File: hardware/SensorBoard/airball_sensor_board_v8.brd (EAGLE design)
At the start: 88.9 x 38.1 mm, 61 parts, among them IC1 CP2102, J2 USB Female Type C Connector, T1 BC846, T2 BC846, U1 BQ24075, U2 BQ27441-G1, U3 BMP388, U4 ESP-WROOM-32, U7 SP0503BAHT

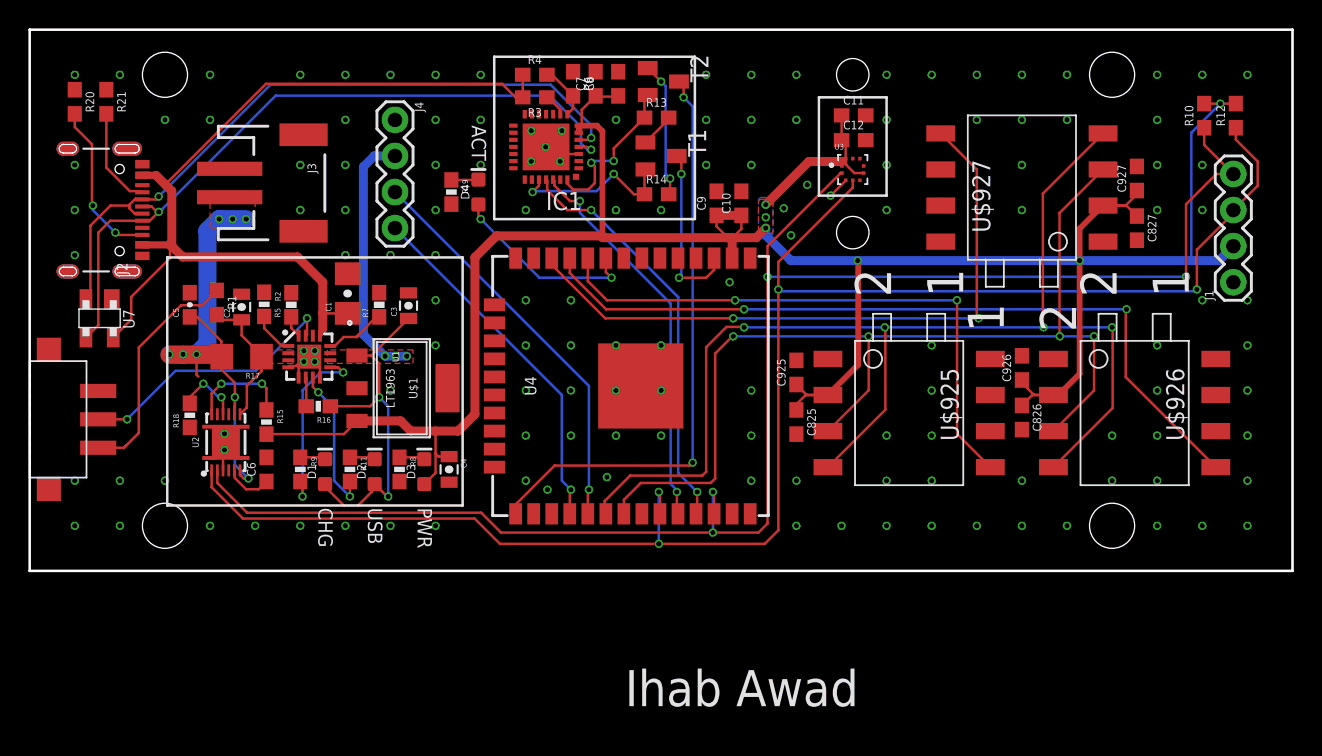
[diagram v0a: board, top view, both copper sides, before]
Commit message: Next rev of sensor board v8
Moved pressure sensors to more accessible location; added a pullup and
capacitor for one of the ESP32 pins for USB access; changed pressure
sensor to the newer BMP390; changed pressure sensor pads to support
either SMD or thru-hole variants; cleaned up the locations of the
barometer and its mounting holes.
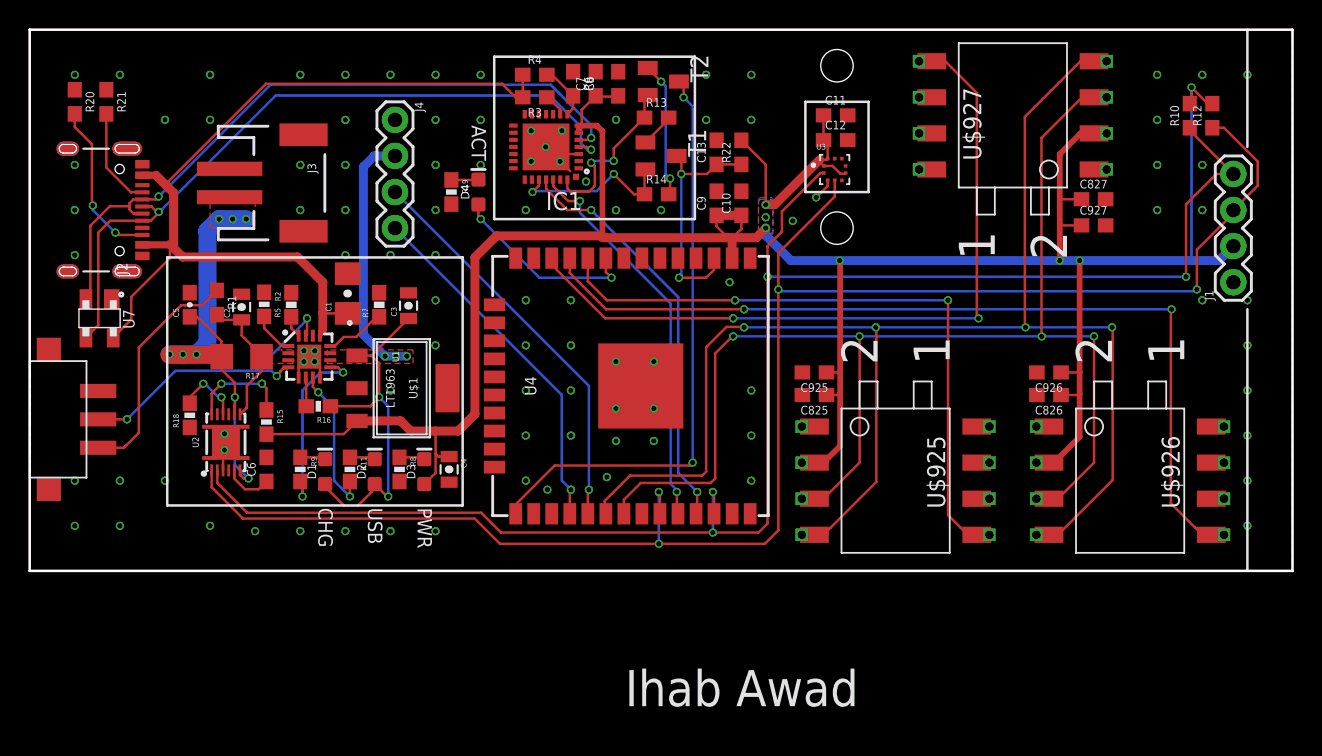
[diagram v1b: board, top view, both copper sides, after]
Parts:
- added C13: 1.0uF, SparkFun-Capacitors:0603
- added R22: 10k, SparkFun-Resistors:0603
- U3: value BMP388 -> BMP390
- moved U$927 5.12 mm to (69.2, 32.1)
- moved U$925 4.86 mm to (61.0, 6.35)
- moved U$926 4.77 mm to (77.5, 6.35)
- moved C927 4.49 mm to (74.9, 24.3), turned to 0 degrees
- moved C827 3.66 mm to (74.9, 26.2), turned to 0 degrees
- moved C826 2.48 mm to (71.8, 12.4), turned to 180 degrees
- moved C825 2.29 mm to (55.2, 12.4), turned to 180 degrees
- moved C926 1.93 mm to (71.8, 14.0), turned to 180 degrees
- moved R12 1.65 mm to (83.3, 32.0)
- moved U3 1.27 mm to (56.7, 28.3)
- moved C11 1.27 mm to (56.7, 32.1)
- moved C12 1.27 mm to (56.7, 30.3)
- moved C925 1.27 mm to (55.2, 14.0), turned to 180 degrees
- moved R10 1.02 mm to (81.7, 32.0)
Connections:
- net EN: now also C13.1, R22.1
- net GND: now also C13.2; no longer U1.4
- net SYSOFF: now also U1.4
- net VCC: now also R22.2
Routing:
- net SCLK: track 85.4 -> 101.9 mm
- net MISO: track 72.7 -> 89.1 mm
- net VCC: track 178.0 -> 189.6 mm, vias 6 -> 7
- net SS_26: track 55.1 -> 62.0 mm
- net SS_27: track 46.2 -> 52.1 mm
- net EN: track 12.3 -> 16.8 mm
- net SS_25: track 40.9 -> 45.3 mm
- net SYSOFF: track 19.0 -> 21.7 mm, vias 2 -> 3
- net BATTERY_IN: track 35.0 -> 33.4 mm
- net GND: track 17.1 -> 18.0 mm, vias 139 -> 98
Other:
- board text removed: "Units in inches"

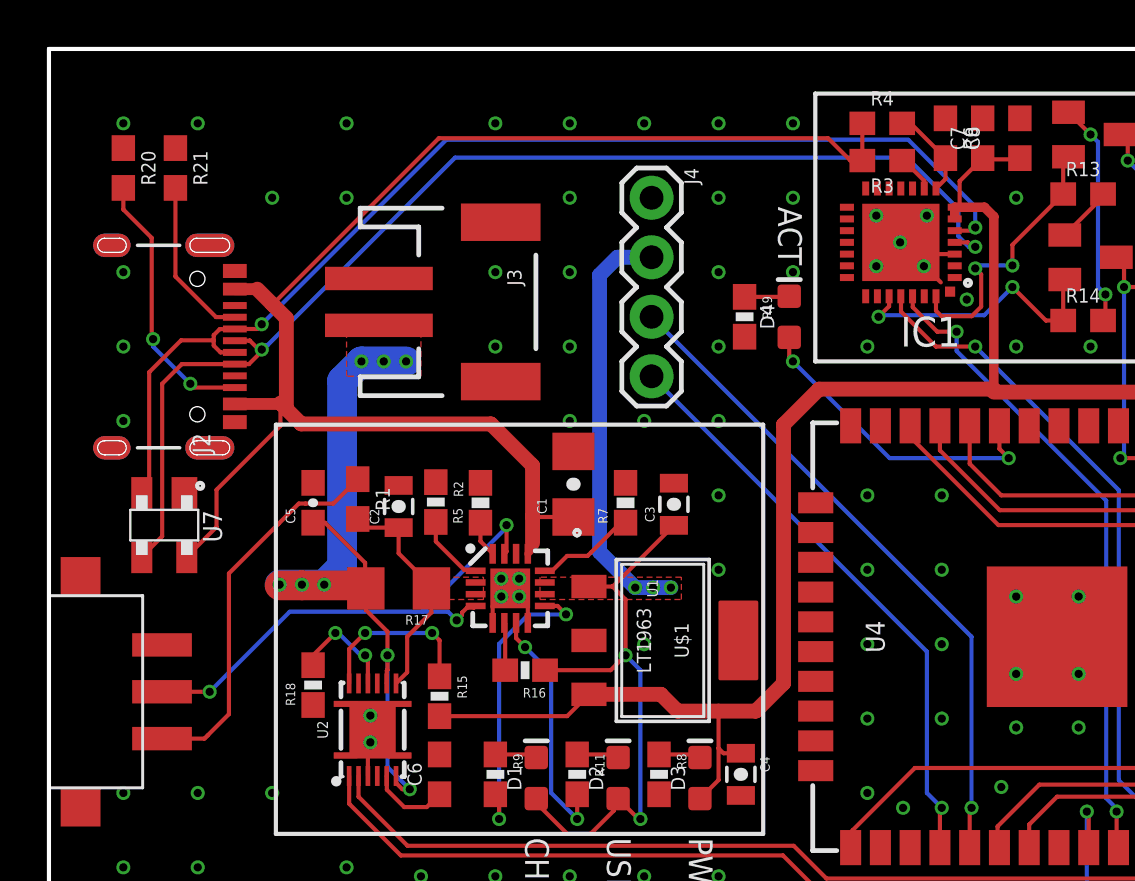
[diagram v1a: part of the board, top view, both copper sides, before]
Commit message: Changed to Molex USB-C connector
Switched to a more readily available Molex USB-C connector.
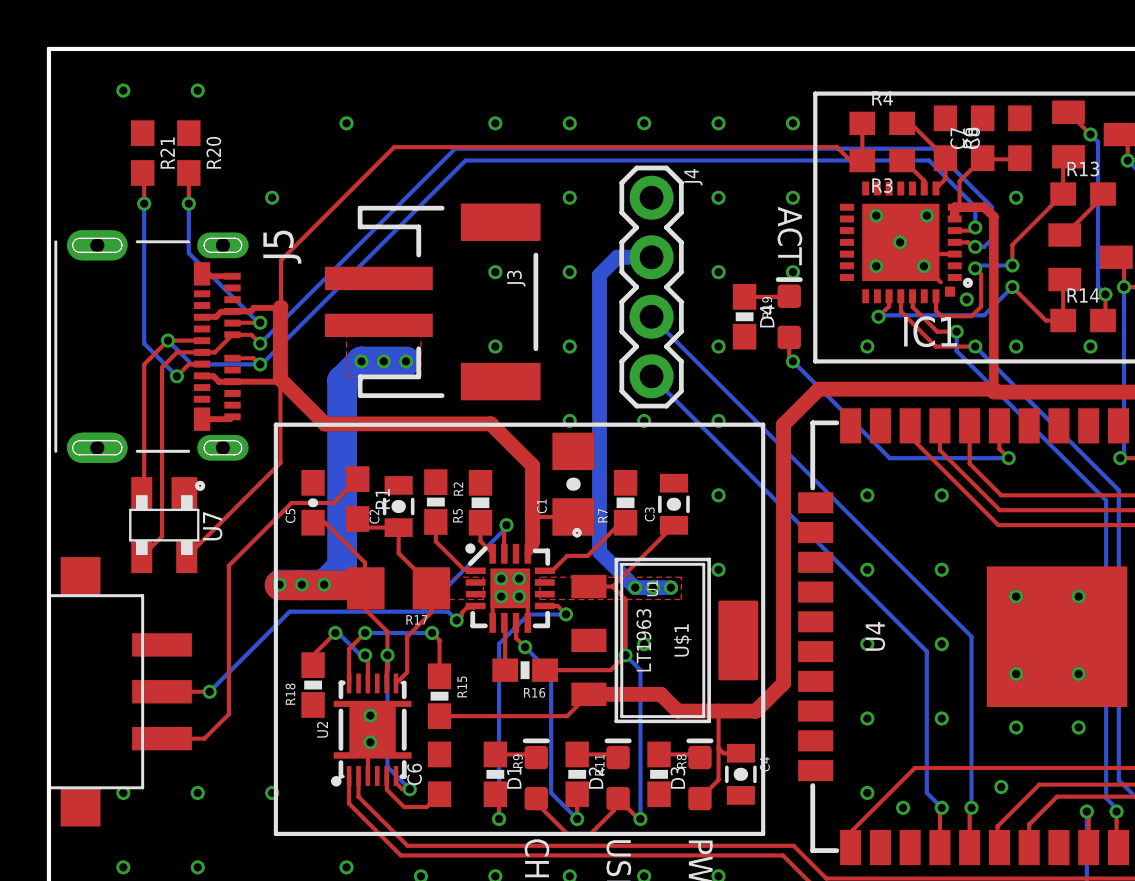
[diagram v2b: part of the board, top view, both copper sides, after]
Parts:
- removed J2: USB Female Type C Connector, SparkFun-Connectors:USB-C-16P
- added J5: 105450-0101, 105450-0101:MOLEX_105450-0101
- moved R20 2.87 mm to (5.97, 33.7)
- moved R21 1.53 mm to (4.00, 33.7)
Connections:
- removed net N$10: J2.B5, R20.2
- removed net N$13: J2.A5, R21.2
- new net USB_CC1: J5.A5, R20.2
- new net USB_CC2: J5.B5, R21.2
- net GND: now also J5.A1, J5.A12, J5.B1, J5.B12, J5.S1, J5.S2, J5.S3, J5.S4; no longer J2.GND, J2.GND2, J2.SHLD1, J2.SHLD2, J2.SHLD3, J2.SHLD4, J2.SHLD5, J2.SHLD6, J2.SHLD7, J2.SHLD8
- net USB_D+: now also J5.A6, J5.B6; no longer J2.A6, J2.B6
- net USB_D-: now also J5.A7, J5.B7; no longer J2.A7, J2.B7
- net V_USB: now also J5.A4, J5.A9, J5.B4, J5.B9; no longer J2.VBUS1, J2.VBUS2
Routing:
- net N$10: track 11.5 -> 0.00 mm, vias 2 -> 0
- net USB_CC2: track 0.00 -> 10.6 mm, vias 0 -> 2
- net USB_CC1: track 0.00 -> 8.89 mm, vias 0 -> 2
- net N$13: track 7.04 -> 0.00 mm
- net V_USB: track 64.3 -> 67.8 mm
- net GND: track 18.0 -> 20.7 mm, vias 98 -> 94
- net USB_D-: track 49.2 -> 50.8 mm, vias 2 -> 3
- net USB_D+: track 51.0 -> 52.2 mm

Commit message: Checkpoint checkin for work in progress on Sensor V8.
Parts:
- moved C11 6.84 mm to (50.4, 29.5), turned to 180 degrees
- moved C12 6.48 mm to (50.4, 31.6), turned to 180 degrees
- moved R22 5.79 mm to (44.5, 28.2), turned to 270 degrees
- moved C13 4.66 mm to (44.5, 32.0)
- moved C10 4.62 mm to (45.7, 24.6), turned to 180 degrees
- moved R19 4.51 mm to (27.3, 30.5), turned to 90 degrees
- moved D4 4.29 mm to (27.3, 26.7)
- moved U3 3.50 mm to (54.0, 30.5)
- moved C8 3.18 mm to (38.3, 34.3)
- moved R3 3.18 mm to (32.4, 33.3)
- moved R4 3.18 mm to (32.4, 34.9)
- moved T1 3.18 mm to (41.3, 29.2)
- moved C7 3.17 mm to (36.7, 34.3)
- moved IC1 3.17 mm to (33.2, 29.8)
- moved R13 3.17 mm to (41.0, 31.9)
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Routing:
- net AUX_RX: track 28.3 -> 32.7 mm
- net N$1: track 13.6 -> 17.9 mm
- net AUX_TX: track 25.3 -> 28.5 mm
- net V_USB: track 67.8 -> 64.7 mm
- net USB_D-: track 50.8 -> 47.7 mm
- net USB_RXD: track 28.9 -> 32.1 mm
- net USB_D+: track 52.2 -> 49.1 mm
- net USB_TXD: track 27.7 -> 30.6 mm
- net VCC: track 189.6 -> 187.1 mm, vias 7 -> 5
- net GND: track 20.7 -> 19.2 mm, vias 94 -> 90
- net IO0: track 41.6 -> 42.9 mm
- net SDA: track 119.2 -> 120.3 mm
- net SCL: track 115.5 -> 116.6 mm
- net EN: track 16.8 -> 17.9 mm
- net V_SUPPLY_UNREG: track 43.9 -> 44.5 mm
- removed copper zone on layer 1, net VCC
- removed copper zone on layer 16, net VCC

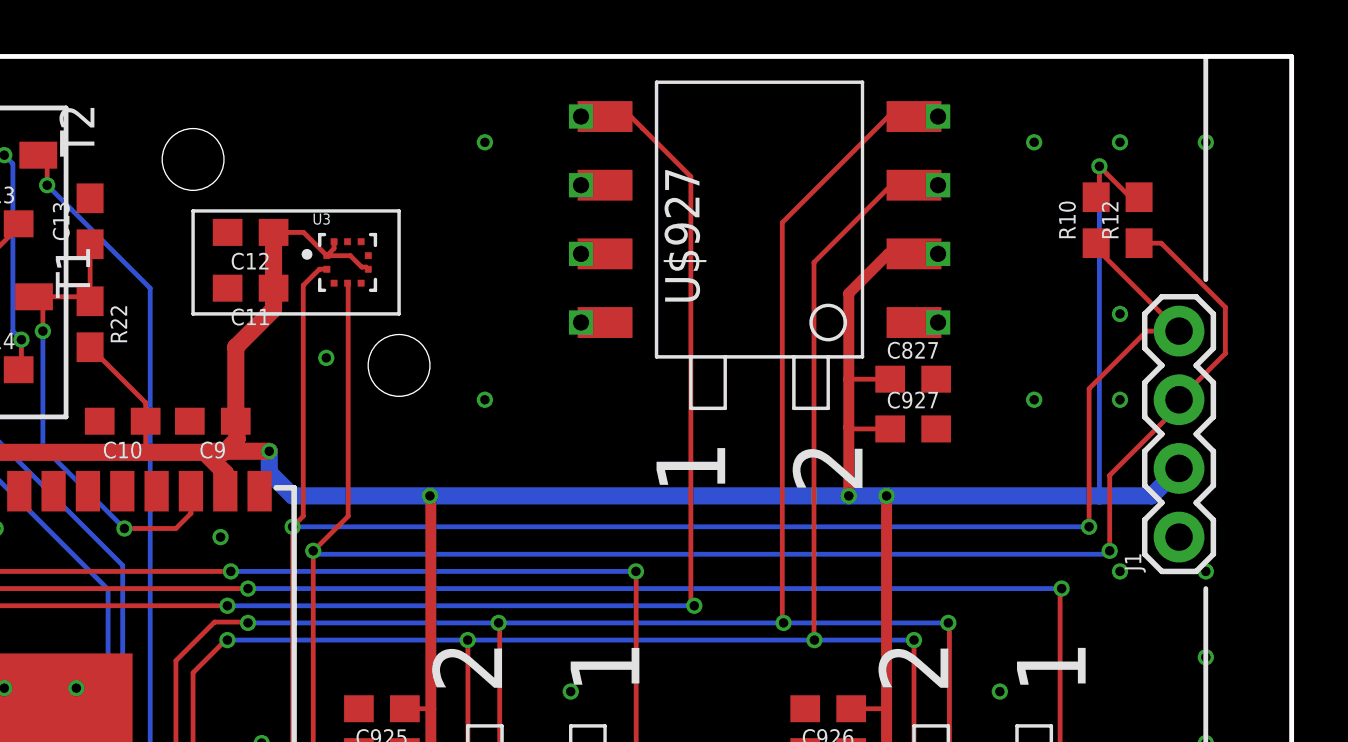
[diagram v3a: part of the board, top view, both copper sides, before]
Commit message: Added QWIIC I2C connector and rearranged a bit.
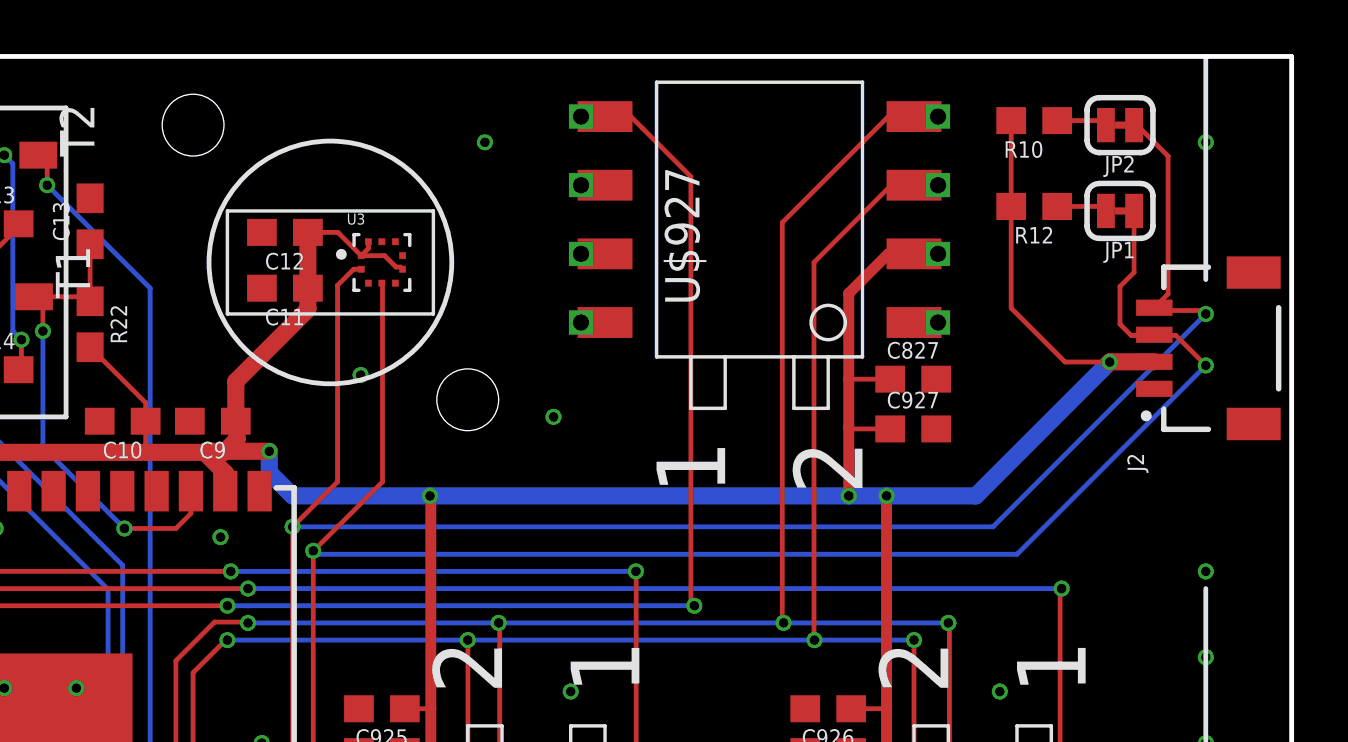
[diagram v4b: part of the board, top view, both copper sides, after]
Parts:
- removed J1: (no value), SparkFun-Connectors:1X04
- added J2: QWIIC_RIGHT_ANGLE, SparkFun-Connectors:JST04_1MM_RA
- added JP1, JP2: JUMPER-SMT_2_NC_TRACE_SILK, SparkFun-Jumpers:SMT-JUMPER_2_NC_TRACE_SILK
- moved R10 4.34 mm to (79.4, 35.7), turned to 180 degrees
- moved R12 3.91 mm to (79.4, 32.6), turned to 180 degrees
- moved C11 1.27 mm to (51.7, 29.5)
- moved C12 1.27 mm to (51.7, 31.6)
- moved U3 1.27 mm to (55.2, 30.5)
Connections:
- new net N$3: JP2.2, R10.1
- new net N$9: JP1.2, R12.1
- net GND: now also J2.1; no longer J1.1
- net SCL: now also J2.4, JP2.1; no longer J1.4, R10.1
- net SDA: now also J2.3, JP1.1; no longer J1.3, R12.1
- net VCC: now also J2.2; no longer J1.2
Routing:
- net SCL: track 116.6 -> 120.5 mm
- net VCC: track 187.1 -> 184.5 mm
- net N$9: track 0.00 -> 1.87 mm
- net N$3: track 0.00 -> 1.87 mm
- net GND: vias 90 -> 84
